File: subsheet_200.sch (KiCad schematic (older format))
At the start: 24 parts, among them J200 DIN-5S — MIDI OUT/THRU, J201 DIN-5S — MIDI IN, U200 MC6850_PHY, U208 PC900_PHY, U210 7406_PHY

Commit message: Removed T-filters
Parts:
- removed L200, L201, L202, L204, L205, L206: EMI_Filter_LCL, commons_passives_THT:Passive_THT_EMI_filter_W5.08mm_L7.62mm, symbol Device:EMI_Filter_LCL
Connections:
- net labels removed: midi_out_1, midi_out_3, midi_out_4, midi_out_5
- wire segments 93 -> 91
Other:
- moved on the sheet: D202, R200, R202, R204, R205, R207, U208

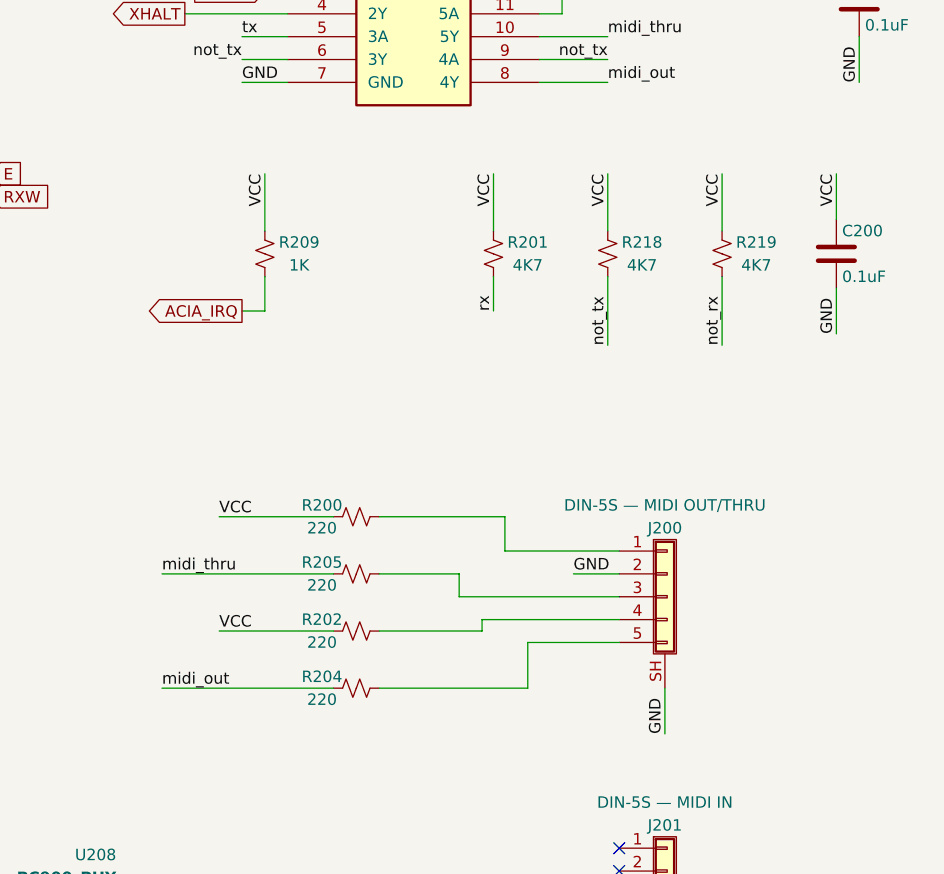
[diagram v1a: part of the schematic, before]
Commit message: Resolves #1 : Use 4-resistor packs wherever it is possible
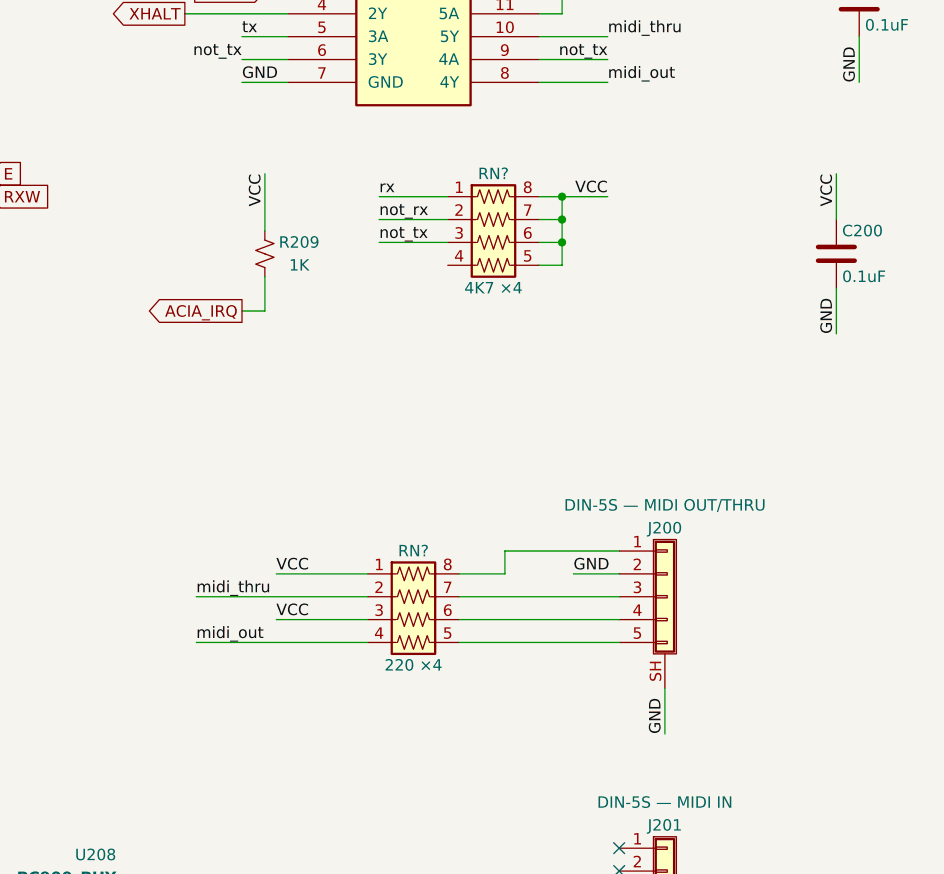
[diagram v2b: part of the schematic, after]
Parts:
- removed R200, R202, R204, R205: 220, commons_passives_THT:Passive_THT_resistor_W2.54mm_L12.70mm, symbol Device:R_Small_US
- removed R201, R218, R219: 4K7, commons_passives_THT:Passive_THT_resistor_W2.54mm_L12.70mm, symbol Device:R_Small_US
- added RN?: 4K7 ×4, symbol custom_passives:R_Pack04_US
- added RN?: 220 ×4, symbol custom_passives:R_Pack04_US
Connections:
- net VCC: now also RN?.1 (R1.1), RN?.3 (R3.1), RN?.5 (R4.2), RN?.6 (R3.2), RN?.7 (R2.2), RN?.8 (R1.2)
- net midi_out: now also RN?.4 (R4.1)
- net midi_thru: now also RN?.2 (R2.1)
- net not_rx: now also RN?.2 (R2.1)
- net not_tx: now also RN?.3 (R3.1)
- net rx: now also RN?.1 (R1.1)
- net at J200.1 (Pin_1): now also RN?.8 (R1.2)
- net at J200.3 (Pin_3): now also RN?.7 (R2.2)
- net at J200.4 (Pin_4): now also RN?.6 (R3.2)
- net at J200.5 (Pin_5): now also RN?.5 (R4.2)
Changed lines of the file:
@@
 Wire Wire Line
 	2450 6350 2650 6350
-$Comp
-L Device:R_Small_US R200
-U 1 1 608F0CAD
-P 4900 4400
-F 0 "R200" V 4850 4250 50  0000 C CNN
-F 1 "220" V 4950 4250 50  0000 C CNN
-F 2 "commons_passives_THT:Passive_THT_resistor_W2.54mm_L12.70mm" H 4900 4400 50  0001 C CNN
-F 3 "~" H 4900 4400 50  0001 C CNN
-	1    4900 4400
-	0    1    1    0
-$EndComp
-$Comp
-L Device:R_Small_US R205
-U 1 1 608F1C5A
-P 4900 4650
-F 0 "R205" V 4850 4500 50  0000 C CNN
-F 1 "220" V 4950 4500 50  0000 C CNN
-F 2 "commons_passives_THT:Passive_THT_resistor_W2.54mm_L12.70mm" H 4900 4650 50  0001 C CNN
-F 3 "~" H 4900 4650 50  0001 C CNN
-	1    4900 4650
-	0    1    1    0
-$EndComp
-$Comp
-L Device:R_Small_US R202
-U 1 1 608F1FF8
-P 4900 4900
-F 0 "R202" V 4850 4750 50  0000 C CNN
-F 1 "220" V 4950 4750 50  0000 C CNN
-F 2 "commons_passives_THT:Passive_THT_resistor_W2.54mm_L12.70mm" H 4900 4900 50  0001 C CNN
-F 3 "~" H 4900 4900 50  0001 C CNN
-	1    4900 4900
-	0    1    1    0
-$EndComp
-$Comp
-L Device:R_Small_US R204
-U 1 1 608F24EF
-P 4900 5150
-F 0 "R204" V 4850 5000 50  0000 C CNN
-F 1 "220" V 4950 5000 50  0000 C CNN
-F 2 "commons_passives_THT:Passive_THT_resistor_W2.54mm_L12.70mm" H 4900 5150 50  0001 C CNN
-F 3 "~" H 4900 5150 50  0001 C CNN
-	1    4900 5150
-	0    1    1    0
-$EndComp
-Text Label 4300 4400 0    50   ~ 0
-VCC
-Text Label 4300 4900 0    50   ~ 0
-VCC
-Text Label 4050 4650 0    50   ~ 0
+Text Label 4550 4650 0    50   ~ 0
+VCC
+Text Label 4550 4850 0    50   ~ 0
+VCC
+Text Label 4200 4750 0    50   ~ 0
 midi_thru
-Text Label 4050 5150 0    50   ~ 0
+Text Label 4200 4950 0    50   ~ 0
 midi_out
 Wire Wire Line
 	5850 4650 6050 4650
-$Comp
-L Device:R_Small_US R218
-U 1 1 608C9942
-P 6000 3250
-F 0 "R218" H 5850 3200 50  0000 C CNN
-F 1 "4K7" H 5850 3300 50  0000 C CNN
-F 2 "commons_passives_THT:Passive_THT_resistor_W2.54mm_L12.70mm" H 6000 3250 50  0001 C CNN
-F 3 "~" H 6000 3250 50  0001 C CNN
-	1    6000 3250
-	-1   0    0    1
-$EndComp
-Text Label 6000 2900 3    50   ~ 0
-VCC
-$Comp
-L Device:R_Small_US R219
-U 1 1 608CBCCA
-P 6500 3250
-F 0 "R219" H 6350 3200 50  0000 C CNN
-F 1 "4K7" H 6350 3300 50  0000 C CNN
-F 2 "commons_passives_THT:Passive_THT_resistor_W2.54mm_L12.70mm" H 6500 3250 50  0001 C CNN
-F 3 "~" H 6500 3250 50  0001 C CNN
-	1    6500 3250
-	-1   0    0    1
-$EndComp
-Text Label 6500 2900 3    50   ~ 0
-VCC
-Text Label 6000 3650 1    50   ~ 0
+Text Label 5000 3200 0    50   ~ 0
 not_tx
-Text Label 6500 3650 1    50   ~ 0
+Text Label 5000 3100 0    50   ~ 0
 not_rx
 $Comp
@@
 	7000 3400 7000 3600
 Wire Wire Line
-	6000 3350 6000 3650
-Wire Wire Line
-	6500 3350 6500 3650
+	5300 3200 5000 3200
+Wire Wire Line
+	5300 3100 5000 3100
 $Comp
 L Device:R_Small_US R207
@@
 Wire Wire Line
 	7100 2300 7100 2500
-Wire Wire Line
-	5500 3350 5500 3500
-Text Label 5500 3500 1    50   ~ 0
+Text Label 5000 3000 0    50   ~ 0
 rx
-Text Label 5500 2900 3    50   ~ 0
-VCC
-$Comp
-L Device:R_Small_US R201
-U 1 1 608C885E
-P 5500 3250
-F 0 "R201" H 5350 3200 50  0000 C CNN
-F 1 "4K7" H 5350 3300 50  0000 C CNN
-F 2 "commons_passives_THT:Passive_THT_resistor_W2.54mm_L12.70mm" H 5500 3250 50  0001 C CNN
-F 3 "~" H 5500 3250 50  0001 C CNN
-	1    5500 3250
-	-1   0    0    1
-$EndComp
 Wire Wire Line
 	3050 2000 3150 2000
@@
 $EndComp
 Wire Wire Line
-	4300 4400 4800 4400
-Wire Wire Line
-	4050 4650 4800 4650
-Wire Wire Line
-	4300 4900 4800 4900
-Wire Wire Line
-	4050 5150 4800 5150
+	4200 4750 4950 4750
+Wire Wire Line
+	4200 4950 4950 4950
 Wire Wire Line
 	4650 6250 4650 6650
@@
 Wire Wire Line
 	5700 1900 6000 1900
-Wire Wire Line
-	5500 2900 5500 3150
-Wire Wire Line
-	6000 2900 6000 3150
-Wire Wire Line
-	6500 2900 6500 3150
 Text Label 6250 5350 1    50   ~ 0
 GND
@@
 	5050 6150 5250 6150
 Wire Wire Line
-	5350 4650 5350 4750
-Wire Wire Line
-	5000 4650 5350 4650
-Wire Wire Line
-	5650 5150 5650 4950
-Wire Wire Line
-	5000 5150 5650 5150
-Wire Wire Line
 	5350 4750 6050 4750
 Wire Wire Line
-	5550 4400 5550 4550
-Wire Wire Line
 	5550 4550 6050 4550
 Wire Wire Line
-	5000 4400 5550 4400
-Wire Wire Line
-	5450 4900 5450 4850
-Wire Wire Line
-	5450 4850 6050 4850
-Wire Wire Line
-	5000 4900 5450 4900
-Wire Wire Line
-	5650 4950 6050 4950
-Wire Wire Line
 	5050 6650 5850 6650
 Wire Wire Line
 	5450 6150 6050 6150
+$Comp
+L custom_passives:R_Pack04_US RN?
+U 1 1 61FA438E
+P 5500 3200
+F 0 "RN?" V 5200 3200 50  0000 C CNN
+F 1 "4K7 ×4" V 5700 3200 50  0000 C CNN
+F 2 "" V 5775 3200 50  0001 C CNN
+F 3 "~" H 5500 3200 50  0001 C CNN
+	1    5500 3200
+	0    1    1    0
+$EndComp
+Text Label 6000 3000 2    50   ~ 0
+VCC
+Wire Wire Line
+	5700 3000 5800 3000
+Wire Wire Line
+	5700 3300 5800 3300
+Wire Wire Line
+	5800 3300 5800 3200
+Connection ~ 5800 3000
+Wire Wire Line
+	5800 3000 6000 3000
+Wire Wire Line
+	5700 3200 5800 3200
+Connection ~ 5800 3200
+Wire Wire Line
+	5800 3200 5800 3100
+Wire Wire Line
+	5700 3100 5800 3100
+Connection ~ 5800 3100
+Wire Wire Line
+	5800 3100 5800 3000
+Wire Wire Line
+	5000 3000 5300 3000
+$Comp
+L custom_passives:R_Pack04_US RN?
+U 1 1 61FBA6ED
+P 5150 4850
+F 0 "RN?" V 4850 4850 50  0000 C CNN
+F 1 "220 ×4" V 5350 4850 50  0000 C CNN
+F 2 "" V 5425 4850 50  0001 C CNN
+F 3 "~" H 5150 4850 50  0001 C CNN
+	1    5150 4850
+	0    1    1    0
+$EndComp
+Wire Wire Line
+	5350 4850 6050 4850
+Wire Wire Line
+	5350 4950 6050 4950
+Wire Wire Line
+	5350 4650 5550 4650
+Wire Wire Line
+	5550 4650 5550 4550
+Wire Wire Line
+	4550 4650 4950 4650
+Wire Wire Line
+	4950 4850 4550 4850
 $EndSCHEMATC

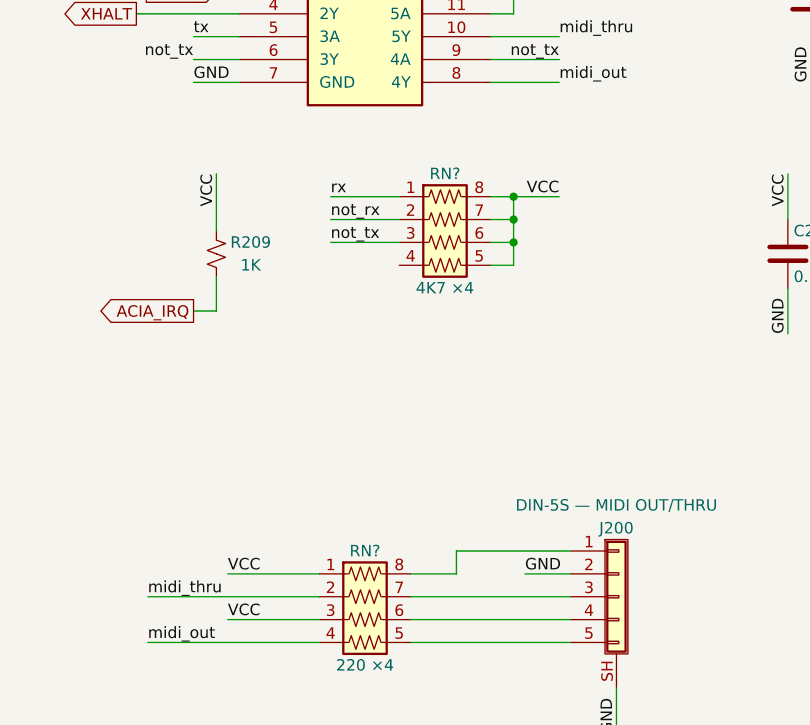
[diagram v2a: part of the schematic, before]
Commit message: annotate resistor networks and mark unused pins as unconnected
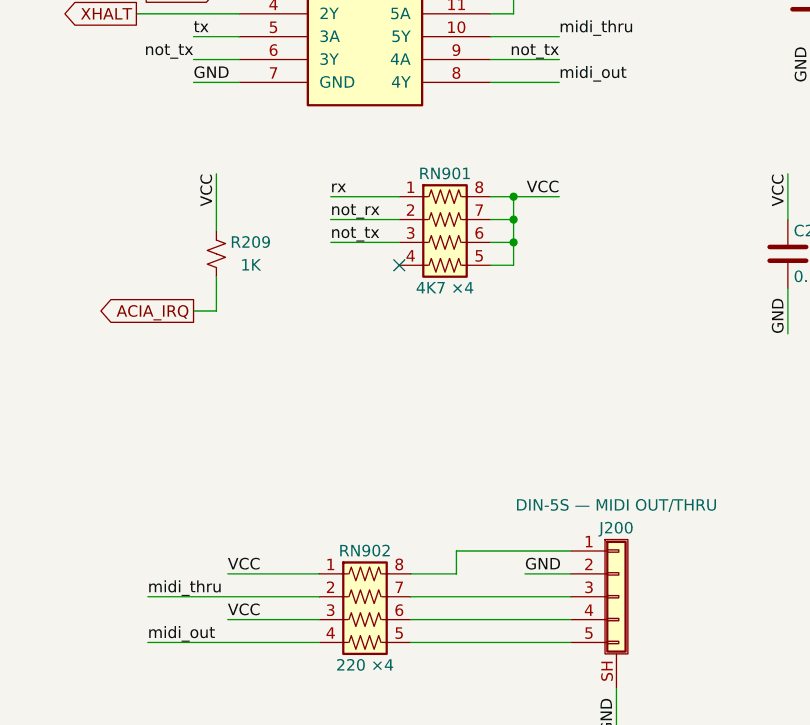
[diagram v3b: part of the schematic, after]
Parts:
- gave numbers to parts that had none: 2
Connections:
- no-connect marks 5 -> 6
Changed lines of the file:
@@
 	5450 6150 6050 6150
 $Comp
-L custom_passives:R_Pack04_US RN?
+L custom_passives:R_Pack04_US RN901
 U 1 1 61FA438E
 P 5500 3200
-F 0 "RN?" V 5200 3200 50  0000 C CNN
+F 0 "RN901" V 5200 3200 50  0000 C CNN
 F 1 "4K7 ×4" V 5700 3200 50  0000 C CNN
 F 2 "" V 5775 3200 50  0001 C CNN
@@
 	5000 3000 5300 3000
 $Comp
-L custom_passives:R_Pack04_US RN?
+L custom_passives:R_Pack04_US RN902
 U 1 1 61FBA6ED
 P 5150 4850
-F 0 "RN?" V 4850 4850 50  0000 C CNN
+F 0 "RN902" V 4850 4850 50  0000 C CNN
 F 1 "220 ×4" V 5350 4850 50  0000 C CNN
 F 2 "" V 5425 4850 50  0001 C CNN
@@
 Wire Wire Line
 	4950 4850 4550 4850
+NoConn ~ 5300 3300
 $EndSCHEMATC

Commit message: Resolves #7 : Assign SMD footprints to resistors pack
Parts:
- RN901, RN902: footprint (none) -> Resistor_SMD:R_Array_Convex_4x0603
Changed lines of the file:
@@
 F 0 "RN901" V 5200 3200 50  0000 C CNN
 F 1 "4K7 ×4" V 5700 3200 50  0000 C CNN
-F 2 "" V 5775 3200 50  0001 C CNN
+F 2 "Resistor_SMD:R_Array_Convex_4x0603" V 5775 3200 50  0001 C CNN
 F 3 "~" H 5500 3200 50  0001 C CNN
 	1    5500 3200
@@
 F 0 "RN902" V 4850 4850 50  0000 C CNN
 F 1 "220 ×4" V 5350 4850 50  0000 C CNN
-F 2 "" V 5425 4850 50  0001 C CNN
+F 2 "Resistor_SMD:R_Array_Convex_4x0603" V 5425 4850 50  0001 C CNN
 F 3 "~" H 5150 4850 50  0001 C CNN
 	1    5150 4850

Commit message: Resolves #13 : assign 1206 hand-solder footprints to resistors
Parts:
- R207, R209: footprint commons_passives_THT:Passive_THT_resistor_W2.54mm_L12.70mm -> Resistor_SMD:R_1206_3216Metric_Pad1.30x1.75mm_HandSolder
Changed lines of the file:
@@
 F 0 "R207" V 5250 6150 50  0000 C CNN
 F 1 "220" V 5450 6150 50  0000 C CNN
-F 2 "commons_passives_THT:Passive_THT_resistor_W2.54mm_L12.70mm" H 5350 6150 50  0001 C CNN
+F 2 "Resistor_SMD:R_1206_3216Metric_Pad1.30x1.75mm_HandSolder" H 5350 6150 50  0001 C CNN
 F 3 "~" H 5350 6150 50  0001 C CNN
 	1    5350 6150
@@
 F 0 "R209" H 4350 3200 50  0000 C CNN
 F 1 "1K" H 4350 3300 50  0000 C CNN
-F 2 "commons_passives_THT:Passive_THT_resistor_W2.54mm_L12.70mm" H 4500 3250 50  0001 C CNN
+F 2 "Resistor_SMD:R_1206_3216Metric_Pad1.30x1.75mm_HandSolder" H 4500 3250 50  0001 C CNN
 F 3 "~" H 4500 3250 50  0001 C CNN
 	1    4500 3250

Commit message: Resolves #8 : Assign 1206 hand-solder footprints to non polarized capacitors
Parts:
- C200, C201, C227: footprint commons_passives_THT:Passive_THT_capacitor_mlcc_W2.54mm_L7.62mm -> Capacitor_SMD:C_1206_3216Metric_Pad1.33x1.80mm_HandSolder
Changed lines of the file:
@@
 F 0 "C200" H 7025 3350 50  0000 L CNN
 F 1 "0.1uF" H 7025 3150 50  0000 L CNN
-F 2 "commons_passives_THT:Passive_THT_capacitor_mlcc_W2.54mm_L7.62mm" H 7038 3100 50  0001 C CNN
+F 2 "Capacitor_SMD:C_1206_3216Metric_Pad1.33x1.80mm_HandSolder" H 7038 3100 50  0001 C CNN
 F 3 "~" H 7000 3250 50  0001 C CNN
 	1    7000 3250
@@
 F 0 "C201" H 1275 3350 50  0000 L CNN
 F 1 "0.1uF" H 1275 3150 50  0000 L CNN
-F 2 "commons_passives_THT:Passive_THT_capacitor_mlcc_W2.54mm_L7.62mm" H 1288 3100 50  0001 C CNN
+F 2 "Capacitor_SMD:C_1206_3216Metric_Pad1.33x1.80mm_HandSolder" H 1288 3100 50  0001 C CNN
 F 3 "~" H 1250 3250 50  0001 C CNN
 	1    1250 3250
@@
 F 0 "C227" H 7125 2250 50  0000 L CNN
 F 1 "0.1uF" H 7125 2050 50  0000 L CNN
-F 2 "commons_passives_THT:Passive_THT_capacitor_mlcc_W2.54mm_L7.62mm" H 7138 2000 50  0001 C CNN
+F 2 "Capacitor_SMD:C_1206_3216Metric_Pad1.33x1.80mm_HandSolder" H 7138 2000 50  0001 C CNN
 F 3 "~" H 7100 2150 50  0001 C CNN
 	1    7100 2150

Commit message: Resolves #16 : assign smd footprints to diodes
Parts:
- D202: footprint commons_passives_THT:Passive_THT_diode_W2.54mm_L12.70mm -> Diode_SMD:D_SOD-123F
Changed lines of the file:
@@
 F 0 "D202" V 5000 6200 50  0000 C CNN
 F 1 "1N914" V 5100 6200 50  0000 C CNN
-F 2 "commons_passives_THT:Passive_THT_diode_W2.54mm_L12.70mm" H 5050 6400 50  0001 C CNN
+F 2 "Diode_SMD:D_SOD-123F" H 5050 6400 50  0001 C CNN
 F 3 "~" H 5050 6400 50  0001 C CNN
 	1    5050 6400
